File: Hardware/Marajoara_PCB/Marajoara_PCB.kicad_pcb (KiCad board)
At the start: 2 copper layers, 256.9 x 207.2 mm, 91 parts, among them J1 Conn_01x03_Socket, Q1 PMOS, Q2 2N7002K, U1 TP4056, U2 ESP32-C3-Supermini

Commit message: Marajoara update
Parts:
- added H1: MountingHole, MountingHole:MountingHole_3.2mm_M3, F.Cu at (166.3, 77.0)
- added H2: MountingHole, MountingHole:MountingHole_3.2mm_M3, F.Cu at (256.2, 76.9)
- added H3: MountingHole, MountingHole:MountingHole_3.2mm_M3, F.Cu at (256.2, 146.9)
- added H4: MountingHole, MountingHole:MountingHole_3.2mm_M3, F.Cu at (166.2, 146.9)
- D1, D10, D11, D12, D13, D14, D15, D16, D17, D18, D19, D2, D20, D21, D22, D23, D24, D25, D26, D27, D28, D3, D4, D5, D6, D7, D8, D9: moved to B.Cu
- R3: value 0R22 -> 220mR 1W 1%; footprint Resistor_SMD:R_2010_5025Metric -> Resistor_SMD:R_1206_3216Metric_Pad1.30x1.75mm_HandSolder
- moved C14 154.5 mm to (106.9, 123.2), turned to 90 degrees
- moved C13 149.8 mm to (122.3, 151.8), turned to 90 degrees
- moved C11 147.1 mm to (176.4, 205.0), turned to 90 degrees
- moved C12 145.2 mm to (147.6, 179.8), turned to -90 degrees
- moved C32 141.5 mm to (204.0, 218.4), turned to 180 degrees
- moved C30 137.5 mm to (203.1, 207.5)
- moved R1 135.4 mm to (152.7, 124.8), turned to 90 degrees
- moved C27 133.9 mm to (203.4, 194.5), turned to 180 degrees
- moved C33 132.3 mm to (219.5, 218.3), turned to 180 degrees
- moved C31 128.3 mm to (218.4, 207.5)
- moved C25 125.9 mm to (203.3, 182.3)
- moved C15 124.4 mm to (142.0, 50.7)
- moved D31 123.4 mm to (160.7, 97.4), turned to 90 degrees
- moved C29 122.2 mm to (218.6, 194.9), turned to 180 degrees
- moved C9 120.9 mm to (252.6, 200.6), turned to -45 degrees
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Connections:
- C11 pad 2: +5V -> V_REG
- C12 pad 2: +5V -> V_REG
- C13 pad 2: +5V -> V_REG
- C14 pad 2: +5V -> V_REG
- C15 pad 2: +5V -> V_REG
- C16 pad 2: +5V -> V_REG
- C17 pad 2: +5V -> V_REG
- C19 pad 2: +5V -> V_REG
- C20 pad 2: +5V -> V_REG
- C21 pad 2: +5V -> V_REG
- C22 pad 2: +5V -> V_REG
- C23 pad 2: +5V -> V_REG
- C24 pad 2: +5V -> V_REG
- C25 pad 2: +5V -> V_REG
- C27 pad 2: +5V -> V_REG
- C28 pad 2: +5V -> V_REG
- C29 pad 2: +5V -> V_REG
- C3 pad 2: +5V -> V_REG
- C30 pad 2: +5V -> V_REG
- C31 pad 2: +5V -> V_REG
- C32 pad 2: +5V -> V_REG
- C33 pad 2: +5V -> V_REG
- C4 pad 2: +5V -> V_REG
- C5 pad 2: +5V -> V_REG
- C6 pad 2: +5V -> V_REG
- C7 pad 2: +5V -> V_REG
- C8 pad 2: +5V -> V_REG
- C9 pad 2: +5V -> V_REG
- D1 pad 3: +5V -> V_REG
- D10 pad 3: +5V -> V_REG
- D11 pad 3: +5V -> V_REG
- D12 pad 3: +5V -> V_REG
- D13 pad 3: +5V -> V_REG
- D14 pad 3: +5V -> V_REG
- D15 pad 3: +5V -> V_REG
- D16 pad 3: +5V -> V_REG
- D17 pad 3: +5V -> V_REG
- D18 pad 3: +5V -> V_REG
- D19 pad 3: +5V -> V_REG
- D2 pad 3: +5V -> V_REG
- D20 pad 3: +5V -> V_REG
- D21 pad 3: +5V -> V_REG
- D22 pad 3: +5V -> V_REG
- D23 pad 3: +5V -> V_REG
- D24 pad 3: +5V -> V_REG
- D25 pad 3: +5V -> V_REG
- D26 pad 3: +5V -> V_REG
- D27 pad 3: +5V -> V_REG
- D28 pad 3: +5V -> V_REG
- D3 pad 3: +5V -> V_REG
- D4 pad 3: +5V -> V_REG
- D5 pad 3: +5V -> V_REG
- D6 pad 3: +5V -> V_REG
- D7 pad 3: +5V -> V_REG
- D8 pad 3: +5V -> V_REG
- D9 pad 3: +5V -> V_REG
- R3 pad 2: Net-(U1-CE) -> Net-(U1-VCC)
- U1 pad 4: Net-(U1-CE) -> Net-(U1-VCC)
- U1 pad 8: Net-(U1-CE) -> +5V
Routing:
- net V_REG: track 0.00 -> 896.9 mm
- net Net-(D18-DOUT): track 0.00 -> 182.6 mm
- net Net-(D1-DOUT): track 0.00 -> 148.4 mm
- net +BATT: track 0.00 -> 139.3 mm
- net Button_GPIO: track 0.00 -> 108.6 mm
- net Net-(D32-K): track 0.00 -> 107.0 mm
- net Net-(Q1-G): track 0.00 -> 102.6 mm
- net Net-(D11-DOUT): track 0.00 -> 94.0 mm
- net Net-(D3-DOUT): track 0.00 -> 93.4 mm
- net Net-(J1-Pin_2): track 0.00 -> 79.6 mm
- net Net-(D2-DOUT): track 0.00 -> 69.3 mm
- net Net-(D12-DOUT): track 0.00 -> 68.3 mm
- net +3.3V: track 0.00 -> 50.1 mm
- net +5V: track 0.00 -> 45.5 mm, vias 0 -> 3
- net Net-(D20-DOUT): track 0.00 -> 37.6 mm
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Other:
- board size 256.9 x 207.2 mm -> 239.5 x 192.5 mm

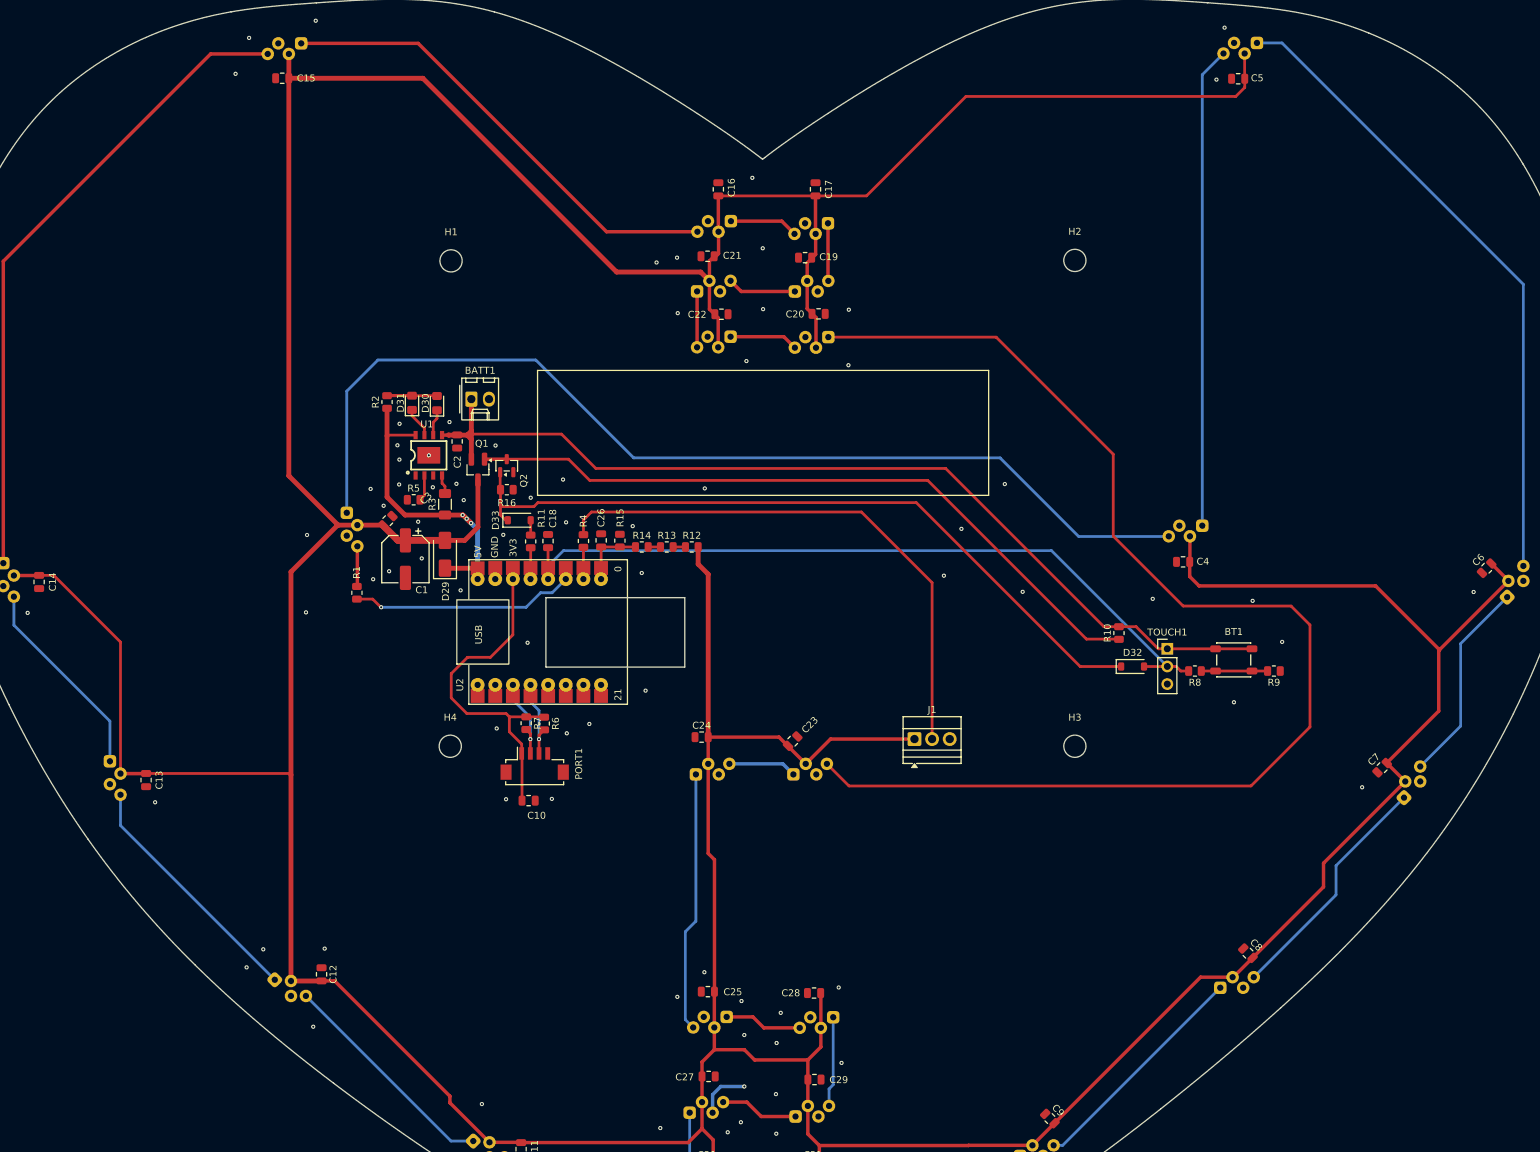
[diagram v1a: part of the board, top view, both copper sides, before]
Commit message: Fabrication files for Marajoara
Plus Xunxo Portabilis, to mend old hardware onto new frame
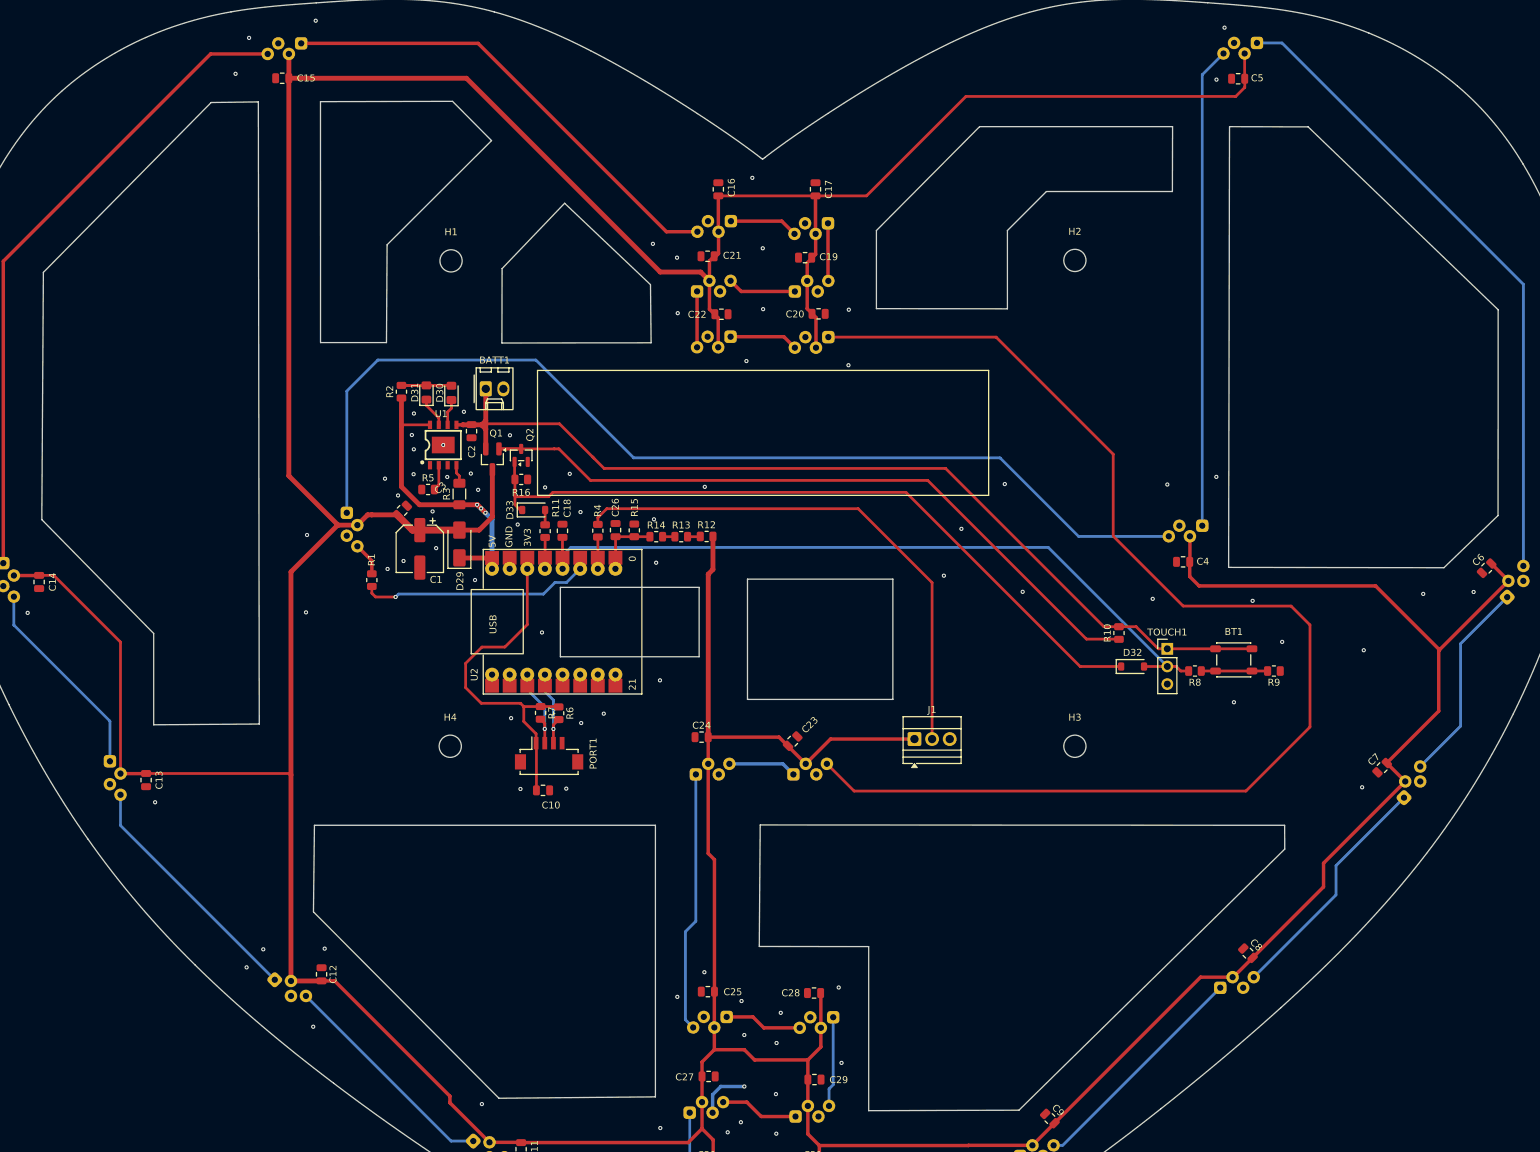
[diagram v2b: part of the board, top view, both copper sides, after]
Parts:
- moved R1 2.82 mm to (154.9, 123.0)
- moved R12 2.62 mm to (203.1, 116.7)
- moved R7 2.55 mm to (179.2, 142.1)
- moved C2 2.55 mm to (169.2, 101.5)
- moved C26 2.55 mm to (190.0, 115.8)
- moved D29 2.55 mm to (167.5, 117.8)
- moved D31 2.55 mm to (162.7, 95.9)
- moved D33 2.55 mm to (178.2, 112.9)
- moved Q1 2.55 mm to (172.2, 105.6)
- moved R15 2.55 mm to (192.7, 115.8)
- moved R16 2.55 mm to (176.4, 108.5)
- moved R3 2.55 mm to (167.5, 110.6)
- moved U1 2.55 mm to (165.2, 103.5)
- moved C18 2.55 mm to (182.3, 115.9)
- moved C3 2.55 mm to (159.2, 112.9)
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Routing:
- net V_REG: track 896.9 -> 900.8 mm
- net Net-(J1-Pin_2): track 79.6 -> 76.6 mm
- net Button_GPIO: track 108.6 -> 106.3 mm
- net Net-(Q1-G): track 102.6 -> 101.1 mm
- net Net-(D32-K): track 107.0 -> 105.6 mm
- net +BATT: track 139.3 -> 138.1 mm
- net Net-(D1-DIN): track 5.87 -> 4.84 mm
- net Majora_out: track 32.3 -> 32.9 mm
- net Net-(D18-DOUT): track 182.6 -> 183.2 mm
- net GND: vias 89 -> 93
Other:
- outline, holes or cut-outs redrawn
